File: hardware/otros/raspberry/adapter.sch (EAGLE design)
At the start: 2 parts

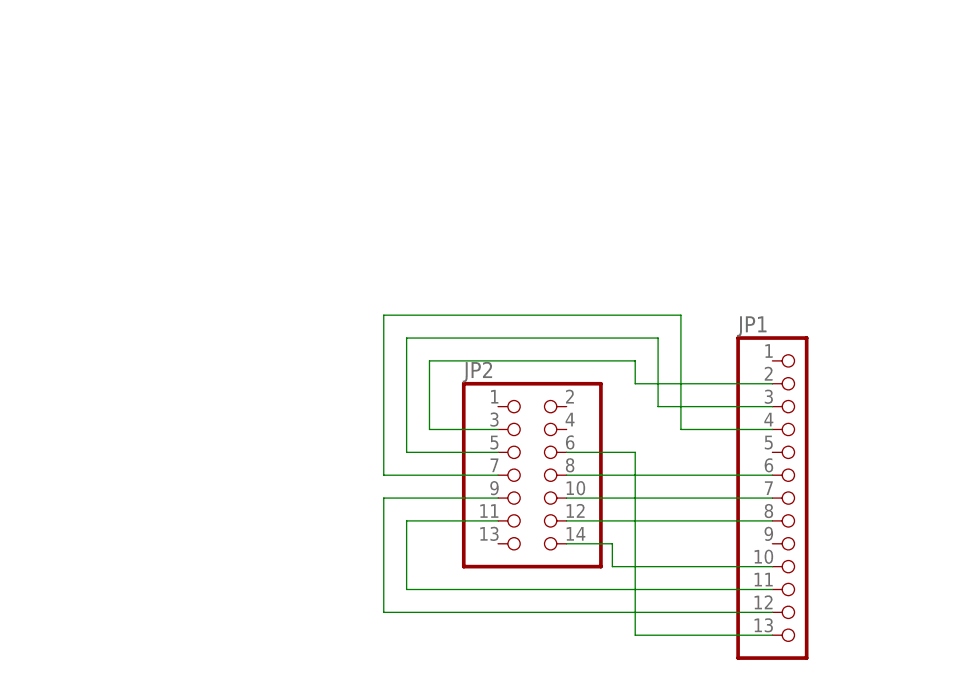
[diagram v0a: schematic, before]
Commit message: 
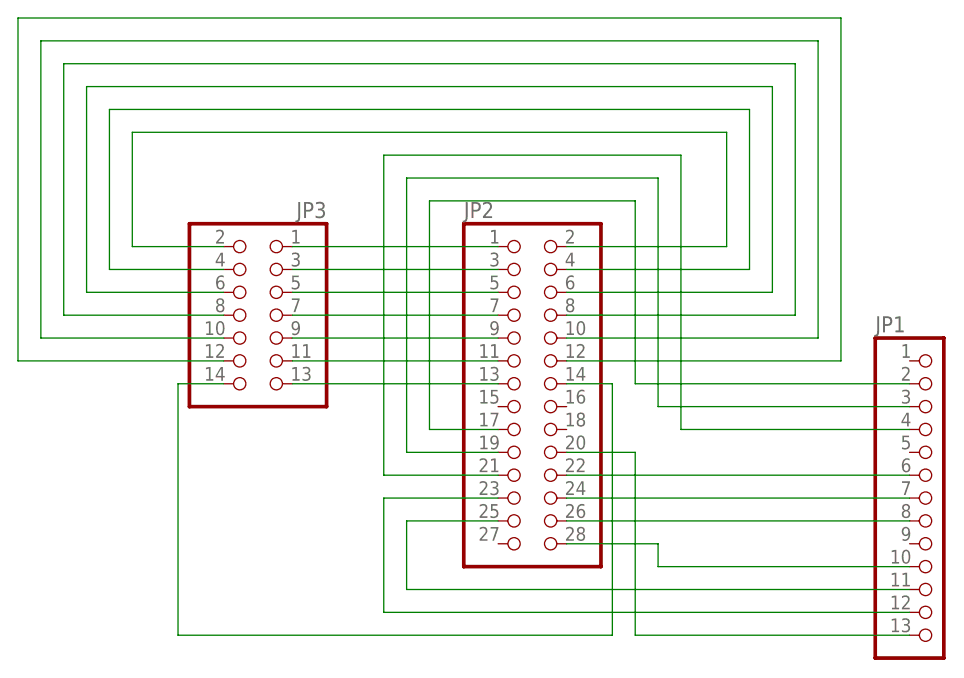
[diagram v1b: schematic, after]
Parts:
- added JP3: (no value), pinhead:PINHD-2X7
- JP2: device pinhead:PINHD-2X7 -> pinhead:PINHD-2X14
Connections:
- new net N$11: JP2.1, JP3.1
- new net N$12: JP2.3, JP3.3
- new net N$13: JP2.5, JP3.5
- new net N$14: JP2.7, JP3.7
- new net N$15: JP2.9, JP3.9
- new net N$16: JP2.11, JP3.11
- new net N$17: JP2.13, JP3.13
- new net N$18: JP2.2, JP3.2
- new net N$19: JP2.4, JP3.4
- new net N$20: JP2.6, JP3.6
- new net N$21: JP2.8, JP3.8
- new net N$22: JP2.10, JP3.10
- new net N$23: JP2.12, JP3.12
- new net N$24: JP2.14, JP3.14
- net N$1: now also JP2.17; no longer JP2.3
- net N$10: now also JP2.22; no longer JP2.8
- net N$2: now also JP2.19; no longer JP2.5
- net N$3: now also JP2.21; no longer JP2.7
- net N$4: now also JP2.23; no longer JP2.9
- net N$5: now also JP2.25; no longer JP2.11
- net N$6: now also JP2.28; no longer JP2.14
- net N$7: now also JP2.26; no longer JP2.12
- net N$8: now also JP2.20; no longer JP2.6
- net N$9: now also JP2.24; no longer JP2.10
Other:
- moved on the sheet: JP1

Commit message: 
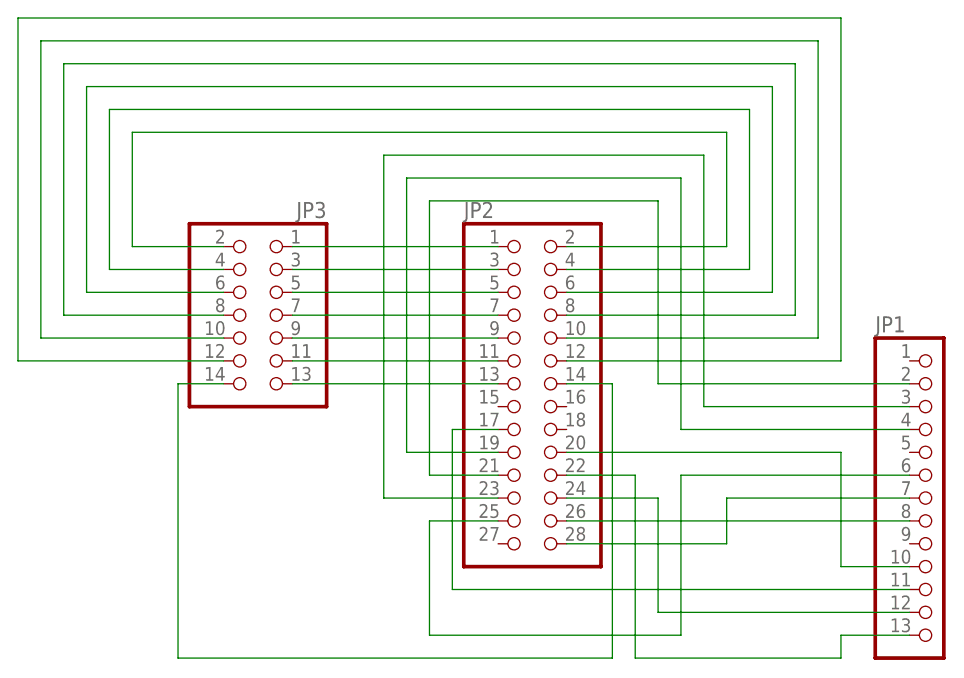
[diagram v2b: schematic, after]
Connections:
- removed net N$1: JP1.2, JP2.17
- new net N$25: JP1.11, JP2.17
- net N$2: now also JP2.23; no longer JP2.19
- net N$3: now also JP2.19; no longer JP2.21
- net N$4: now also JP2.24; no longer JP2.23
- net N$5: now also JP1.7, JP2.28; no longer JP1.11, JP2.25
- net N$6: now also JP2.20; no longer JP2.28
- net N$8: now also JP1.2, JP2.21; no longer JP1.6, JP2.20
- net N$9: now also JP1.6, JP2.25; no longer JP1.7, JP2.24
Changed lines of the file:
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@@
 </busses>
 <nets>
-<net name="N$1" class="0">
-<segment>
-<wire x1="22.86" y1="63.5" x2="15.24" y2="63.5" width="0.1524" layer="91"/>
-<wire x1="15.24" y1="63.5" x2="15.24" y2="88.9" width="0.1524" layer="91"/>
-<wire x1="15.24" y1="88.9" x2="38.1" y2="88.9" width="0.1524" layer="91"/>
-<wire x1="38.1" y1="88.9" x2="38.1" y2="68.58" width="0.1524" layer="91"/>
-<pinref part="JP1" gate="A" pin="2"/>
-<wire x1="68.58" y1="68.58" x2="38.1" y2="68.58" width="0.1524" layer="91"/>
-<pinref part="JP2" gate="A" pin="17"/>
-</segment>
-</net>
-<net name="N$2" class="0">
-<segment>
-<wire x1="22.86" y1="60.96" x2="12.7" y2="60.96" width="0.1524" layer="91"/>
-<wire x1="12.7" y1="60.96" x2="12.7" y2="91.44" width="0.1524" layer="91"/>
-<wire x1="12.7" y1="91.44" x2="40.64" y2="91.44" width="0.1524" layer="91"/>
-<wire x1="40.64" y1="91.44" x2="40.64" y2="66.04" width="0.1524" layer="91"/>
-<pinref part="JP1" gate="A" pin="3"/>
-<wire x1="40.64" y1="66.04" x2="68.58" y2="66.04" width="0.1524" layer="91"/>
-<pinref part="JP2" gate="A" pin="19"/>
-</segment>
-</net>
 <net name="N$3" class="0">
 <segment>
-<wire x1="22.86" y1="58.42" x2="10.16" y2="58.42" width="0.1524" layer="91"/>
-<wire x1="10.16" y1="58.42" x2="10.16" y2="93.98" width="0.1524" layer="91"/>
-<wire x1="10.16" y1="93.98" x2="43.18" y2="93.98" width="0.1524" layer="91"/>
+<wire x1="12.7" y1="91.44" x2="43.18" y2="91.44" width="0.1524" layer="91"/>
 <pinref part="JP1" gate="A" pin="4"/>
 <wire x1="43.18" y1="63.5" x2="68.58" y2="63.5" width="0.1524" layer="91"/>
-<wire x1="43.18" y1="93.98" x2="43.18" y2="63.5" width="0.1524" layer="91"/>
-<pinref part="JP2" gate="A" pin="21"/>
+<wire x1="43.18" y1="91.44" x2="43.18" y2="63.5" width="0.1524" layer="91"/>
+<pinref part="JP2" gate="A" pin="19"/>
+<wire x1="22.86" y1="60.96" x2="12.7" y2="60.96" width="0.1524" layer="91"/>
+<wire x1="12.7" y1="91.44" x2="12.7" y2="60.96" width="0.1524" layer="91"/>
 </segment>
 </net>
 <net name="N$4" class="0">
 <segment>
-<wire x1="22.86" y1="55.88" x2="10.16" y2="55.88" width="0.1524" layer="91"/>
-<wire x1="10.16" y1="55.88" x2="10.16" y2="43.18" width="0.1524" layer="91"/>
 <pinref part="JP1" gate="A" pin="12"/>
-<wire x1="10.16" y1="43.18" x2="68.58" y2="43.18" width="0.1524" layer="91"/>
-<pinref part="JP2" gate="A" pin="23"/>
-</segment>
-</net>
-<net name="N$5" class="0">
-<segment>
-<wire x1="22.86" y1="53.34" x2="12.7" y2="53.34" width="0.1524" layer="91"/>
-<wire x1="12.7" y1="53.34" x2="12.7" y2="45.72" width="0.1524" layer="91"/>
-<pinref part="JP1" gate="A" pin="11"/>
-<wire x1="12.7" y1="45.72" x2="68.58" y2="45.72" width="0.1524" layer="91"/>
-<pinref part="JP2" gate="A" pin="25"/>
+<pinref part="JP2" gate="A" pin="24"/>
+<wire x1="40.64" y1="43.18" x2="68.58" y2="43.18" width="0.1524" layer="91"/>
+<wire x1="30.48" y1="55.88" x2="40.64" y2="55.88" width="0.1524" layer="91"/>
+<wire x1="40.64" y1="55.88" x2="40.64" y2="43.18" width="0.1524" layer="91"/>
 </segment>
 </net>
 <net name="N$6" class="0">
 <segment>
-<wire x1="30.48" y1="50.8" x2="40.64" y2="50.8" width="0.1524" layer="91"/>
-<wire x1="40.64" y1="50.8" x2="40.64" y2="48.26" width="0.1524" layer="91"/>
 <pinref part="JP1" gate="A" pin="10"/>
-<wire x1="40.64" y1="48.26" x2="68.58" y2="48.26" width="0.1524" layer="91"/>
-<pinref part="JP2" gate="A" pin="28"/>
+<wire x1="60.96" y1="48.26" x2="68.58" y2="48.26" width="0.1524" layer="91"/>
+<wire x1="30.48" y1="60.96" x2="60.96" y2="60.96" width="0.1524" layer="91"/>
+<pinref part="JP2" gate="A" pin="20"/>
+<wire x1="60.96" y1="60.96" x2="60.96" y2="48.26" width="0.1524" layer="91"/>
 </segment>
 </net>
@@
 <wire x1="30.48" y1="53.34" x2="68.58" y2="53.34" width="0.1524" layer="91"/>
 <pinref part="JP2" gate="A" pin="26"/>
-</segment>
-</net>
-<net name="N$8" class="0">
-<segment>
-<wire x1="30.48" y1="60.96" x2="38.1" y2="60.96" width="0.1524" layer="91"/>
-<wire x1="38.1" y1="60.96" x2="38.1" y2="58.42" width="0.1524" layer="91"/>
-<pinref part="JP1" gate="A" pin="6"/>
-<wire x1="38.1" y1="58.42" x2="68.58" y2="58.42" width="0.1524" layer="91"/>
-<pinref part="JP2" gate="A" pin="20"/>
-</segment>
-</net>
-<net name="N$9" class="0">
-<segment>
-<pinref part="JP1" gate="A" pin="7"/>
-<wire x1="30.48" y1="55.88" x2="68.58" y2="55.88" width="0.1524" layer="91"/>
-<pinref part="JP2" gate="A" pin="24"/>
-</segment>
-</net>
-<net name="N$10" class="0">
-<segment>
-<wire x1="30.48" y1="58.42" x2="38.1" y2="58.42" width="0.1524" layer="91"/>
-<wire x1="38.1" y1="58.42" x2="38.1" y2="40.64" width="0.1524" layer="91"/>
-<pinref part="JP1" gate="A" pin="13"/>
-<wire x1="38.1" y1="40.64" x2="68.58" y2="40.64" width="0.1524" layer="91"/>
-<pinref part="JP2" gate="A" pin="22"/>
 </segment>
 </net>
@@
 <pinref part="JP2" gate="A" pin="14"/>
 <wire x1="30.48" y1="68.58" x2="35.56" y2="68.58" width="0.1524" layer="91"/>
-<wire x1="35.56" y1="68.58" x2="35.56" y2="40.64" width="0.1524" layer="91"/>
-<wire x1="35.56" y1="40.64" x2="-12.7" y2="40.64" width="0.1524" layer="91"/>
-<wire x1="-12.7" y1="40.64" x2="-12.7" y2="68.58" width="0.1524" layer="91"/>
+<wire x1="35.56" y1="68.58" x2="35.56" y2="38.1" width="0.1524" layer="91"/>
+<wire x1="35.56" y1="38.1" x2="-12.7" y2="38.1" width="0.1524" layer="91"/>
+<wire x1="-12.7" y1="38.1" x2="-12.7" y2="68.58" width="0.1524" layer="91"/>
 <pinref part="JP3" gate="A" pin="14"/>
 <wire x1="-12.7" y1="68.58" x2="-7.62" y2="68.58" width="0.1524" layer="91"/>
 </segment>
 </net>
+<net name="N$25" class="0">
+<segment>
+<pinref part="JP2" gate="A" pin="17"/>
+<wire x1="22.86" y1="63.5" x2="17.78" y2="63.5" width="0.1524" layer="91"/>
+<pinref part="JP1" gate="A" pin="11"/>
+<wire x1="17.78" y1="45.72" x2="68.58" y2="45.72" width="0.1524" layer="91"/>
+<wire x1="17.78" y1="63.5" x2="17.78" y2="45.72" width="0.1524" layer="91"/>
+</segment>
+</net>
+<net name="N$8" class="0">
+<segment>
+<pinref part="JP1" gate="A" pin="2"/>
+<wire x1="68.58" y1="68.58" x2="40.64" y2="68.58" width="0.1524" layer="91"/>
+<wire x1="15.24" y1="88.9" x2="40.64" y2="88.9" width="0.1524" layer="91"/>
+<wire x1="40.64" y1="68.58" x2="40.64" y2="88.9" width="0.1524" layer="91"/>
+<pinref part="JP2" gate="A" pin="21"/>
+<wire x1="22.86" y1="58.42" x2="15.24" y2="58.42" width="0.1524" layer="91"/>
+<wire x1="15.24" y1="88.9" x2="15.24" y2="58.42" width="0.1524" layer="91"/>
+</segment>
+</net>
+<net name="N$9" class="0">
+<segment>
+<pinref part="JP2" gate="A" pin="25"/>
+<wire x1="22.86" y1="53.34" x2="15.24" y2="53.34" width="0.1524" layer="91"/>
+<wire x1="15.24" y1="53.34" x2="15.24" y2="40.64" width="0.1524" layer="91"/>
+<wire x1="15.24" y1="40.64" x2="43.18" y2="40.64" width="0.1524" layer="91"/>
+<pinref part="JP1" gate="A" pin="6"/>
+<wire x1="43.18" y1="58.42" x2="68.58" y2="58.42" width="0.1524" layer="91"/>
+<wire x1="43.18" y1="40.64" x2="43.18" y2="58.42" width="0.1524" layer="91"/>
+</segment>
+</net>
+<net name="N$5" class="0">
+<segment>
+<wire x1="30.48" y1="50.8" x2="48.26" y2="50.8" width="0.1524" layer="91"/>
+<pinref part="JP2" gate="A" pin="28"/>
+<pinref part="JP1" gate="A" pin="7"/>
+<wire x1="68.58" y1="55.88" x2="48.26" y2="55.88" width="0.1524" layer="91"/>
+<wire x1="48.26" y1="50.8" x2="48.26" y2="55.88" width="0.1524" layer="91"/>
+</segment>
+</net>
+<net name="N$2" class="0">
+<segment>
+<pinref part="JP2" gate="A" pin="23"/>
+<wire x1="22.86" y1="55.88" x2="10.16" y2="55.88" width="0.1524" layer="91"/>
+<wire x1="10.16" y1="93.98" x2="45.72" y2="93.98" width="0.1524" layer="91"/>
+<wire x1="45.72" y1="93.98" x2="45.72" y2="66.04" width="0.1524" layer="91"/>
+<pinref part="JP1" gate="A" pin="3"/>
+<wire x1="45.72" y1="66.04" x2="68.58" y2="66.04" width="0.1524" layer="91"/>
+<wire x1="10.16" y1="55.88" x2="10.16" y2="93.98" width="0.1524" layer="91"/>
+</segment>
+</net>
+<net name="N$26" class="0">
+<segment>
+<wire x1="30.48" y1="58.42" x2="38.1" y2="58.42" width="0.1524" layer="91"/>
+<pinref part="JP2" gate="A" pin="22"/>
+<pinref part="JP1" gate="A" pin="13"/>
+<wire x1="68.58" y1="40.64" x2="60.96" y2="40.64" width="0.1524" layer="91"/>
+<wire x1="60.96" y1="40.64" x2="60.96" y2="38.1" width="0.1524" layer="91"/>
+<wire x1="60.96" y1="38.1" x2="38.1" y2="38.1" width="0.1524" layer="91"/>
+<wire x1="38.1" y1="58.42" x2="38.1" y2="38.1" width="0.1524" layer="91"/>
+</segment>
+</net>

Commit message: 
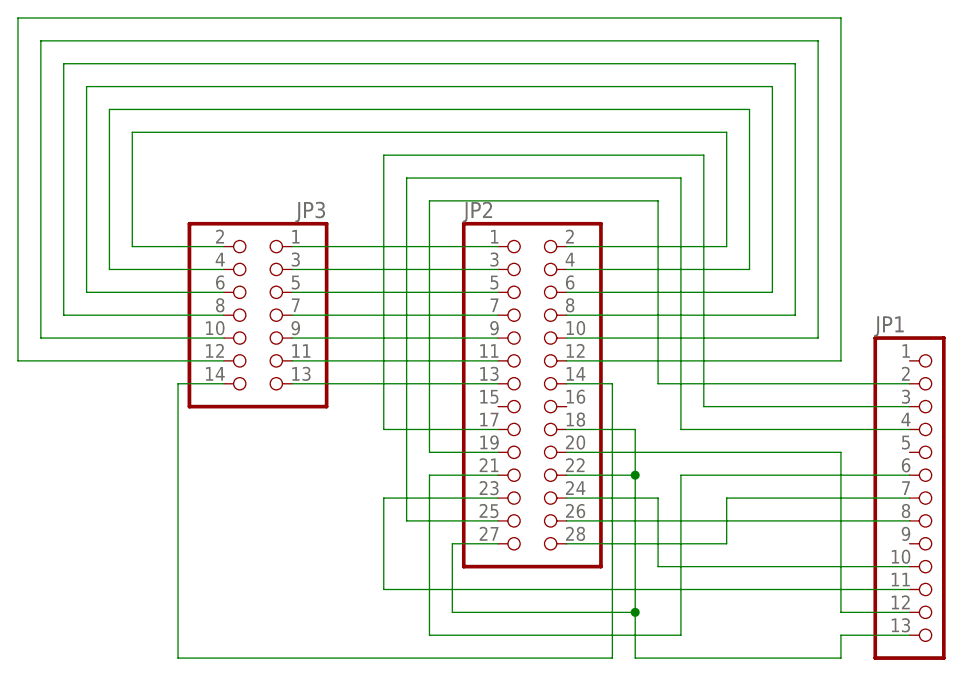
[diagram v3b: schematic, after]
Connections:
- removed net N$26: JP1.13, JP2.22
- removed net N$4: JP1.12, JP2.24
- new net GND: JP1.13, JP2.18, JP2.22, JP2.27
- new net N$10: JP1.11, JP2.23
- net N$2: now also JP2.17; no longer JP2.23
- net N$25: now also JP1.10, JP2.24; no longer JP1.11, JP2.17
- net N$3: now also JP2.25; no longer JP2.19
- net N$6: now also JP1.12; no longer JP1.10
- net N$8: now also JP2.19; no longer JP2.21
- net N$9: now also JP2.21; no longer JP2.25
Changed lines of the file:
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@@
 <wire x1="43.18" y1="63.5" x2="68.58" y2="63.5" width="0.1524" layer="91"/>
 <wire x1="43.18" y1="91.44" x2="43.18" y2="63.5" width="0.1524" layer="91"/>
-<pinref part="JP2" gate="A" pin="19"/>
-<wire x1="22.86" y1="60.96" x2="12.7" y2="60.96" width="0.1524" layer="91"/>
-<wire x1="12.7" y1="91.44" x2="12.7" y2="60.96" width="0.1524" layer="91"/>
-</segment>
-</net>
-<net name="N$4" class="0">
-<segment>
-<pinref part="JP1" gate="A" pin="12"/>
-<pinref part="JP2" gate="A" pin="24"/>
-<wire x1="40.64" y1="43.18" x2="68.58" y2="43.18" width="0.1524" layer="91"/>
-<wire x1="30.48" y1="55.88" x2="40.64" y2="55.88" width="0.1524" layer="91"/>
-<wire x1="40.64" y1="55.88" x2="40.64" y2="43.18" width="0.1524" layer="91"/>
+<pinref part="JP2" gate="A" pin="25"/>
+<wire x1="22.86" y1="53.34" x2="12.7" y2="53.34" width="0.1524" layer="91"/>
+<wire x1="12.7" y1="91.44" x2="12.7" y2="53.34" width="0.1524" layer="91"/>
 </segment>
 </net>
 <net name="N$6" class="0">
 <segment>
-<pinref part="JP1" gate="A" pin="10"/>
-<wire x1="60.96" y1="48.26" x2="68.58" y2="48.26" width="0.1524" layer="91"/>
 <wire x1="30.48" y1="60.96" x2="60.96" y2="60.96" width="0.1524" layer="91"/>
 <pinref part="JP2" gate="A" pin="20"/>
-<wire x1="60.96" y1="60.96" x2="60.96" y2="48.26" width="0.1524" layer="91"/>
+<pinref part="JP1" gate="A" pin="12"/>
+<wire x1="60.96" y1="43.18" x2="68.58" y2="43.18" width="0.1524" layer="91"/>
+<wire x1="60.96" y1="60.96" x2="60.96" y2="43.18" width="0.1524" layer="91"/>
 </segment>
 </net>
@@
 </segment>
 </net>
-<net name="N$25" class="0">
-<segment>
-<pinref part="JP2" gate="A" pin="17"/>
-<wire x1="22.86" y1="63.5" x2="17.78" y2="63.5" width="0.1524" layer="91"/>
-<pinref part="JP1" gate="A" pin="11"/>
-<wire x1="17.78" y1="45.72" x2="68.58" y2="45.72" width="0.1524" layer="91"/>
-<wire x1="17.78" y1="63.5" x2="17.78" y2="45.72" width="0.1524" layer="91"/>
-</segment>
-</net>
 <net name="N$8" class="0">
 <segment>
@@
 <wire x1="15.24" y1="88.9" x2="40.64" y2="88.9" width="0.1524" layer="91"/>
 <wire x1="40.64" y1="68.58" x2="40.64" y2="88.9" width="0.1524" layer="91"/>
-<pinref part="JP2" gate="A" pin="21"/>
-<wire x1="22.86" y1="58.42" x2="15.24" y2="58.42" width="0.1524" layer="91"/>
-<wire x1="15.24" y1="88.9" x2="15.24" y2="58.42" width="0.1524" layer="91"/>
+<wire x1="15.24" y1="88.9" x2="15.24" y2="60.96" width="0.1524" layer="91"/>
+<pinref part="JP2" gate="A" pin="19"/>
+<wire x1="15.24" y1="60.96" x2="22.86" y2="60.96" width="0.1524" layer="91"/>
 </segment>
 </net>
 <net name="N$9" class="0">
 <segment>
-<pinref part="JP2" gate="A" pin="25"/>
-<wire x1="22.86" y1="53.34" x2="15.24" y2="53.34" width="0.1524" layer="91"/>
-<wire x1="15.24" y1="53.34" x2="15.24" y2="40.64" width="0.1524" layer="91"/>
 <wire x1="15.24" y1="40.64" x2="43.18" y2="40.64" width="0.1524" layer="91"/>
 <pinref part="JP1" gate="A" pin="6"/>
 <wire x1="43.18" y1="58.42" x2="68.58" y2="58.42" width="0.1524" layer="91"/>
 <wire x1="43.18" y1="40.64" x2="43.18" y2="58.42" width="0.1524" layer="91"/>
+<pinref part="JP2" gate="A" pin="21"/>
+<wire x1="15.24" y1="58.42" x2="22.86" y2="58.42" width="0.1524" layer="91"/>
+<wire x1="15.24" y1="40.64" x2="15.24" y2="58.42" width="0.1524" layer="91"/>
 </segment>
 </net>
@@
 <net name="N$2" class="0">
 <segment>
-<pinref part="JP2" gate="A" pin="23"/>
-<wire x1="22.86" y1="55.88" x2="10.16" y2="55.88" width="0.1524" layer="91"/>
 <wire x1="10.16" y1="93.98" x2="45.72" y2="93.98" width="0.1524" layer="91"/>
 <wire x1="45.72" y1="93.98" x2="45.72" y2="66.04" width="0.1524" layer="91"/>
 <pinref part="JP1" gate="A" pin="3"/>
 <wire x1="45.72" y1="66.04" x2="68.58" y2="66.04" width="0.1524" layer="91"/>
-<wire x1="10.16" y1="55.88" x2="10.16" y2="93.98" width="0.1524" layer="91"/>
-</segment>
-</net>
-<net name="N$26" class="0">
+<wire x1="10.16" y1="93.98" x2="10.16" y2="63.5" width="0.1524" layer="91"/>
+<pinref part="JP2" gate="A" pin="17"/>
+<wire x1="10.16" y1="63.5" x2="22.86" y2="63.5" width="0.1524" layer="91"/>
+</segment>
+</net>
+<net name="GND" class="0">
 <segment>
 <wire x1="30.48" y1="58.42" x2="38.1" y2="58.42" width="0.1524" layer="91"/>
@@
 <wire x1="60.96" y1="40.64" x2="60.96" y2="38.1" width="0.1524" layer="91"/>
 <wire x1="60.96" y1="38.1" x2="38.1" y2="38.1" width="0.1524" layer="91"/>
-<wire x1="38.1" y1="58.42" x2="38.1" y2="38.1" width="0.1524" layer="91"/>
-</segment>
-</net>
+<wire x1="38.1" y1="58.42" x2="38.1" y2="43.18" width="0.1524" layer="91"/>
+<wire x1="38.1" y1="43.18" x2="38.1" y2="38.1" width="0.1524" layer="91"/>
+<wire x1="38.1" y1="58.42" x2="38.1" y2="63.5" width="0.1524" layer="91"/>
+<junction x="38.1" y="58.42"/>
+<pinref part="JP2" gate="A" pin="18"/>
+<wire x1="38.1" y1="63.5" x2="30.48" y2="63.5" width="0.1524" layer="91"/>
+<pinref part="JP2" gate="A" pin="27"/>
+<wire x1="22.86" y1="50.8" x2="17.78" y2="50.8" width="0.1524" layer="91"/>
+<wire x1="17.78" y1="50.8" x2="17.78" y2="43.18" width="0.1524" layer="91"/>
+<wire x1="17.78" y1="43.18" x2="38.1" y2="43.18" width="0.1524" layer="91"/>
+<junction x="38.1" y="43.18"/>
+</segment>
+</net>
+<net name="N$10" class="0">
+<segment>
+<pinref part="JP2" gate="A" pin="23"/>
+<wire x1="22.86" y1="55.88" x2="10.16" y2="55.88" width="0.1524" layer="91"/>
+<wire x1="10.16" y1="55.88" x2="10.16" y2="45.72" width="0.1524" layer="91"/>
+<pinref part="JP1" gate="A" pin="11"/>
+<wire x1="10.16" y1="45.72" x2="68.58" y2="45.72" width="0.1524" layer="91"/>
+</segment>
+</net>
+<net name="N$25" class="0">
+<segment>
+<pinref part="JP2" gate="A" pin="24"/>
+<wire x1="30.48" y1="55.88" x2="40.64" y2="55.88" width="0.1524" layer="91"/>
+<wire x1="40.64" y1="55.88" x2="40.64" y2="48.26" width="0.1524" layer="91"/>
+<pinref part="JP1" gate="A" pin="10"/>
+<wire x1="40.64" y1="48.26" x2="68.58" y2="48.26" width="0.1524" layer="91"/>
+</segment>
+</net>
